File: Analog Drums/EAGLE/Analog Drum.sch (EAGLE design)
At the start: 78 parts, among them IC1 LM741P, IC2 LM741P, IC3 LM741P, IC4 LM741P, IC5 LM741P, Q1 2N3906, Q2 2N3906, T2 2N3904, T3 2N3904, T4 2N3904

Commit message: I think im done
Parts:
- C13: value 40n -> 47n
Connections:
- removed net POT2_3: T4.C
- net POT1: now also T4.C
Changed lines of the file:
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@@
 <part name="IC4" library="linear" library_urn="urn:adsk.eagle:library:262" deviceset="*741" device="P" package3d_urn="urn:adsk.eagle:package:16409/2" technology="LM"/>
 <part name="IC5" library="linear" library_urn="urn:adsk.eagle:library:262" deviceset="*741" device="P" package3d_urn="urn:adsk.eagle:package:16409/2" technology="LM"/>
-<part name="C13" library="resistor" library_urn="urn:adsk.eagle:library:348" deviceset="C-EU" device="050-024X044" package3d_urn="urn:adsk.eagle:package:26162/1" value="40n"/>
+<part name="C13" library="resistor" library_urn="urn:adsk.eagle:library:348" deviceset="C-EU" device="050-024X044" package3d_urn="urn:adsk.eagle:package:26162/1" value="47n"/>
 <part name="R24" library="resistor" library_urn="urn:adsk.eagle:library:348" deviceset="R-US_" device="0207/10" package3d_urn="urn:adsk.eagle:package:25939/1" value="47k"/>
 <part name="R25" library="resistor" library_urn="urn:adsk.eagle:library:348" deviceset="R-US_" device="0207/10" package3d_urn="urn:adsk.eagle:package:25939/1" value="22k"/>
@@
 </segment>
 </net>
-<net name="POT2_3" class="0">
-<segment>
-<pinref part="T4" gate="G1" pin="C"/>
-<label x="167.64" y="157.48" size="1.778" layer="95" rot="R180"/>
-<wire x1="167.64" y1="149.86" x2="167.64" y2="154.94" width="0.1524" layer="91"/>
-</segment>
-</net>
 <net name="SW3" class="0">
 <segment>
@@
 <label x="109.22" y="50.8" size="1.778" layer="95"/>
 </segment>
-</net>
+<segment>
+<pinref part="T4" gate="G1" pin="C"/>
+<label x="167.64" y="157.48" size="1.778" layer="95" rot="R180"/>
+<wire x1="167.64" y1="149.86" x2="167.64" y2="154.94" width="0.1524" layer="91"/>
+</segment>
+</net>

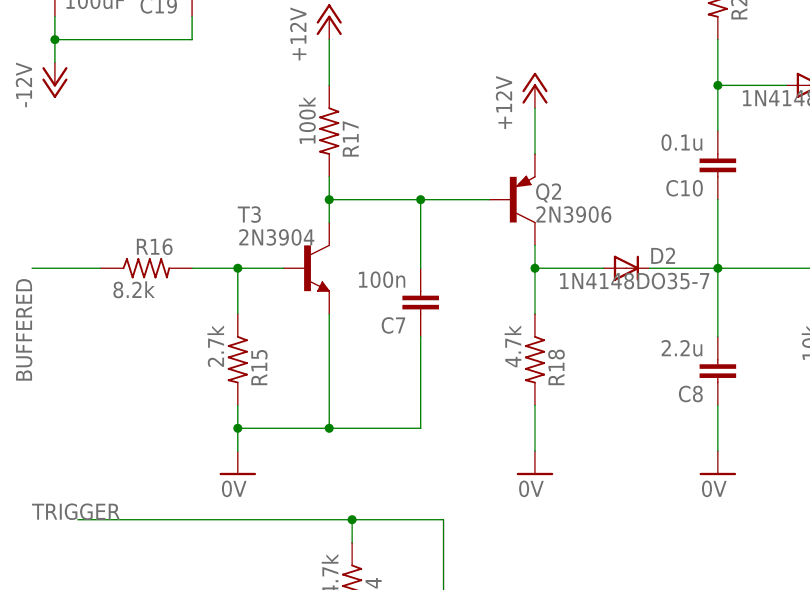
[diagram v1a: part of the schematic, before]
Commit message: Added 100ohm resistor
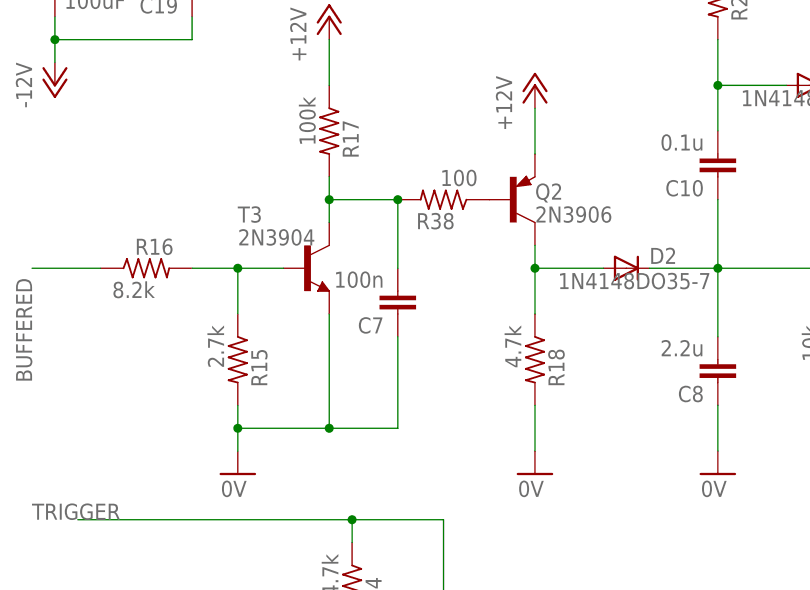
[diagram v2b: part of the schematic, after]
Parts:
- added R38: 100, resistor:R-US_0207/10
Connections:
- new net N$5: Q2.B, R38.1
- net N$14: now also R38.2; no longer Q2.B
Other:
- moved on the sheet: C7
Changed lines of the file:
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@@
 <?xml version="1.0" encoding="utf-8"?>
 <!DOCTYPE eagle SYSTEM "eagle.dtd">
-<eagle version="9.2.2">
+<eagle version="9.3.1">
 <drawing>
 <settings>
@@
 <part name="C24" library="rcl" library_urn="urn:adsk.eagle:library:334" deviceset="CPOL-US" device="E2.5-6" package3d_urn="urn:adsk.eagle:package:23349/1" value="10uF"/>
 <part name="C26" library="resistor" library_urn="urn:adsk.eagle:library:348" deviceset="C-EU" device="050-024X044" package3d_urn="urn:adsk.eagle:package:26162/1" value="100n"/>
+<part name="R38" library="resistor" library_urn="urn:adsk.eagle:library:348" deviceset="R-US_" device="0207/10" package3d_urn="urn:adsk.eagle:package:25939/1" value="100"/>
 </parts>
 <sheets>
@@
 <attribute name="VALUE" x="50.8" y="167.64" size="1.778" layer="96" rot="R90"/>
 </instance>
-<instance part="C7" gate="G$1" x="63.5" y="139.7" smashed="yes" rot="R180">
-<attribute name="NAME" x="61.976" y="139.319" size="1.778" layer="95" rot="R180"/>
-<attribute name="VALUE" x="61.976" y="144.399" size="1.778" layer="96" rot="R180"/>
+<instance part="C7" gate="G$1" x="60.96" y="139.7" smashed="yes" rot="R180">
+<attribute name="NAME" x="59.436" y="139.319" size="1.778" layer="95" rot="R180"/>
+<attribute name="VALUE" x="59.436" y="144.399" size="1.778" layer="96" rot="R180"/>
 </instance>
 <instance part="Q2" gate="G$1" x="73.66" y="152.4" smashed="yes">
@@
 <attribute name="NAME" x="67.056" y="63.119" size="1.778" layer="95" rot="R180"/>
 <attribute name="VALUE" x="67.056" y="68.199" size="1.778" layer="96" rot="R180"/>
+</instance>
+<instance part="R38" gate="G$1" x="66.04" y="152.4" smashed="yes" rot="R180">
+<attribute name="NAME" x="67.31" y="150.9014" size="1.778" layer="95" rot="R180"/>
+<attribute name="VALUE" x="69.85" y="155.702" size="1.778" layer="96" rot="R180"/>
 </instance>
 </instances>
@@
 <junction x="43.18" y="127"/>
 <pinref part="C7" gate="G$1" pin="1"/>
-<wire x1="63.5" y1="137.16" x2="63.5" y2="127" width="0.1524" layer="91"/>
-<wire x1="63.5" y1="127" x2="53.34" y2="127" width="0.1524" layer="91"/>
+<wire x1="60.96" y1="137.16" x2="60.96" y2="127" width="0.1524" layer="91"/>
+<wire x1="60.96" y1="127" x2="53.34" y2="127" width="0.1524" layer="91"/>
 <junction x="53.34" y="127"/>
 </segment>
@@
 <wire x1="53.34" y1="154.94" x2="53.34" y2="152.4" width="0.1524" layer="91"/>
 <wire x1="53.34" y1="152.4" x2="53.34" y2="149.86" width="0.1524" layer="91"/>
-<wire x1="53.34" y1="152.4" x2="63.5" y2="152.4" width="0.1524" layer="91"/>
+<wire x1="53.34" y1="152.4" x2="60.96" y2="152.4" width="0.1524" layer="91"/>
 <junction x="53.34" y="152.4"/>
 <pinref part="C7" gate="G$1" pin="2"/>
-<wire x1="63.5" y1="152.4" x2="63.5" y2="144.78" width="0.1524" layer="91"/>
-<pinref part="Q2" gate="G$1" pin="B"/>
-<wire x1="63.5" y1="152.4" x2="71.12" y2="152.4" width="0.1524" layer="91"/>
-<junction x="63.5" y="152.4"/>
+<wire x1="60.96" y1="152.4" x2="60.96" y2="144.78" width="0.1524" layer="91"/>
+<pinref part="R38" gate="G$1" pin="2"/>
+<junction x="60.96" y="152.4"/>
 </segment>
 </net>
@@
 </segment>
 </net>
+<net name="N$5" class="0">
+<segment>
+<pinref part="Q2" gate="G$1" pin="B"/>
+<pinref part="R38" gate="G$1" pin="1"/>
+</segment>
+</net>
